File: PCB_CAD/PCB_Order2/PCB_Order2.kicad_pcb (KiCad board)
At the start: 4 copper layers, 48 parts, among them U1 SN74AXCH1T45DCKR, U2 SN74AXCH1T45DCKR

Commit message: moved some stuff on pcb
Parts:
- moved DigitalIn1 99.0 mm to (70.5, 81.7), turned to -90 degrees
- moved C1 90.2 mm to (98.1, 104.6)
- moved C2 90.2 mm to (98.1, 107.6)
- moved C3 90.2 mm to (98.1, 110.6)
- moved C4 90.2 mm to (98.1, 113.6)
- moved C5 90.2 mm to (98.1, 116.6)
- moved C6 90.2 mm to (98.1, 119.6)
- moved C7 90.2 mm to (98.1, 122.6)
- moved C8 90.2 mm to (103.0, 104.6)
- moved DacAnalogSupply_bulk1 90.2 mm to (103.0, 107.6)
- moved DacAnalogSupply_noise1 90.2 mm to (103.0, 110.6)
- moved DacMute_CurrentLimit1 90.2 mm to (102.7, 125.4)
- moved DacOut_L_decouple1 90.2 mm to (103.0, 113.6)
- moved DacOut_L_res1 90.2 mm to (102.7, 127.9)
- moved DacOut_R_decouple1 90.2 mm to (103.0, 116.6)
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
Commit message: continued progress on pcb design
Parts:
- FLASH1, LLSin_ACcouple1, RAM1, SPDIFTX1, SpdifOut_AcCoupling1, SpdifOut_ImpedanceMatch1, llsOut_refHi_noise2, llsOut_refLo_noise1, llsOut_refLo_noise2, uController1: moved to B.Cu
- LLS In1: renamed from U1; moved to B.Cu
- LLS Out1: renamed from U2; moved to B.Cu
- moved AnalogOut1 110.7 mm to (60.5, 131.2), turned to 180 degrees
- moved RAM1 95.3 mm to (141.5, 129.0), turned to 180 degrees
- moved SPDIFTX1 81.1 mm to (140.5, 146.8), turned to 180 degrees
- moved DigitalIn1 80.2 mm to (110.0, 151.5), turned to 180 degrees
- moved AnalogIn1 77.9 mm to (71.5, 146.8), turned to -90 degrees
- moved DigitalOut1 77.3 mm to (125.0, 151.5), turned to 180 degrees
- moved uController1 69.3 mm to (118.5, 129.0), turned to 180 degrees
- moved ADC1 66.9 mm to (100.0, 120.5)
- moved DAC1 64.8 mm to (100.5, 110.0)
- moved SpdifOut_ImpedanceMatch1 54.7 mm to (125.0, 149.5), turned to -90 degrees
- moved Dac_DigitalSup_bulk1 43.5 mm to (86.8, 66.5)
- moved Dac_DigitalSup_noise2 43.5 mm to (86.8, 75.5)
- moved dixSupply_bulk1 43.5 mm to (91.6, 66.5)
- moved C4 43.5 mm to (77.2, 75.5)
- moved C8 43.5 mm to (82.0, 66.5)
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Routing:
- net Net-(DAC1-VREF): track 0.00 -> 9.76 mm
- net Net-(ADC1-VCOM): track 0.00 -> 6.56 mm
- net VDD: track 0.00 -> 4.67 mm, vias 0 -> 1
- net VDD_DIV: track 0.00 -> 4.59 mm
- net GNDD: vias 0 -> 5
- added copper zone on In2.Cu, net (none)
- added copper zone on In2.Cu, net GNDA
- added copper zone on In2.Cu, net GNDD
- added copper zone on In1.Cu, net VDD
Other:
- board outline added: 105.5 x 57 mm
- board text added: "GNDA"
- board text added: "GNDD"

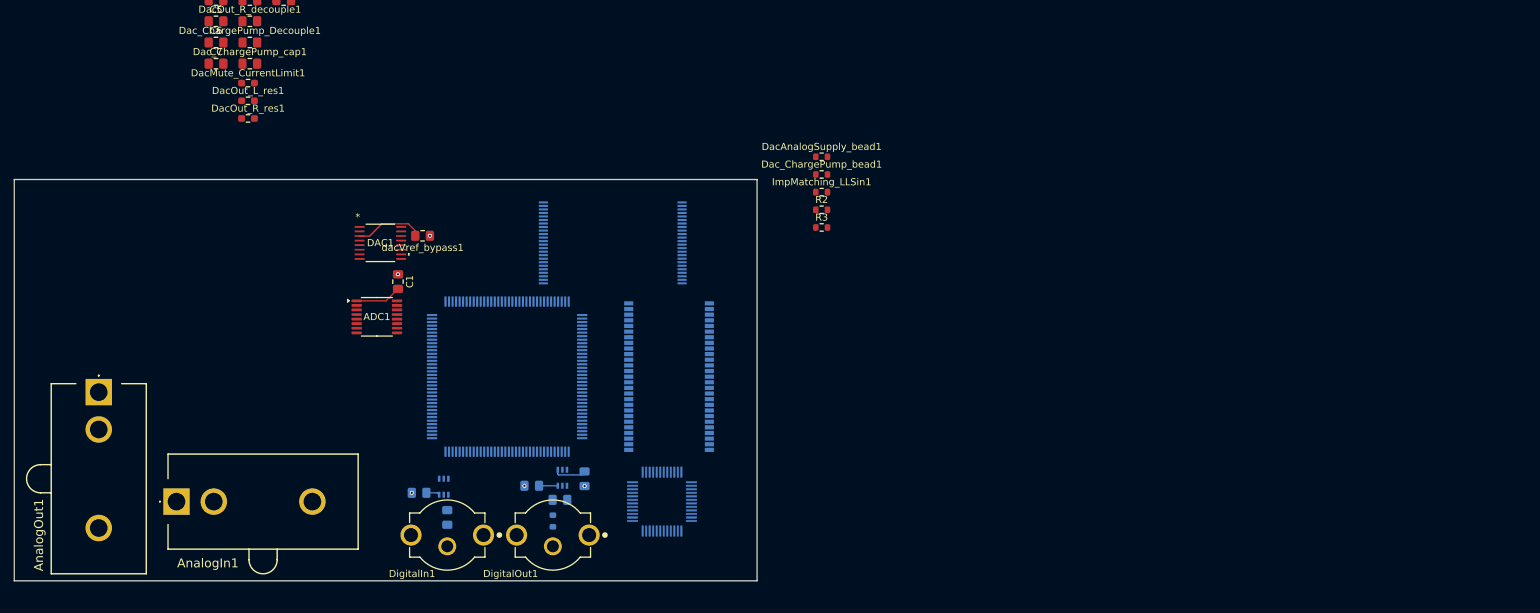
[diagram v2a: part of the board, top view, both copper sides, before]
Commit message: more pcb design things. RAM and Flash wiring
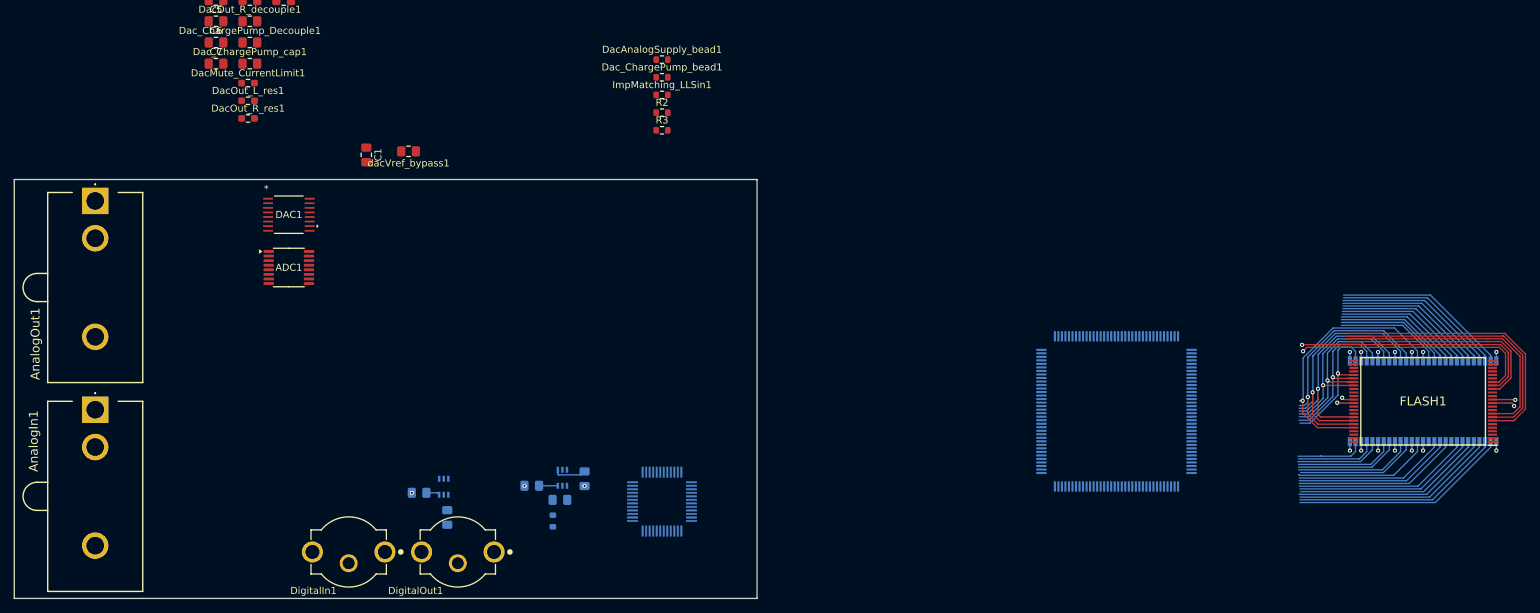
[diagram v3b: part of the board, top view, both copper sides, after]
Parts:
- FLASH1: moved to F.Cu
- moved FLASH1 117.3 mm to (248.6, 132.5), turned to 180 degrees
- moved RAM1 107.2 mm to (248.6, 132.5), turned to -90 degrees
- moved uController1 86.7 mm to (205.1, 133.9), turned to 0 degrees
- moved AnalogOut1 27.2 mm to (60.0, 104.0)
- moved ImpMatching_LLSin1 26.5 mm to (140.5, 89.0)
- moved DacAnalogSupply_bead1 26.5 mm to (140.5, 84.0)
- moved Dac_ChargePump_bead1 26.5 mm to (140.5, 86.5)
- moved R2 26.5 mm to (140.5, 91.5)
- moved R3 26.5 mm to (140.5, 94.0)
- moved C1 18.6 mm to (98.5, 97.5)
- moved AnalogIn1 17.4 mm to (60.0, 133.7), turned to 180 degrees
- moved ADC1 14.3 mm to (87.5, 113.5)
- moved DigitalIn1 14.2 mm to (96.0, 153.9)
- moved DigitalOut1 13.7 mm to (111.5, 153.9)
- moved DAC1 13.6 mm to (87.5, 106.0)
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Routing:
- net /FMC_NWAIT: track 0.00 -> 39.7 mm
- net /FMC_NOE: track 0.00 -> 38.5 mm
- net /FMC_NCE: track 0.00 -> 37.2 mm
- net /FMC_D7: track 0.00 -> 37.1 mm, vias 0 -> 1
- net /FMC_ALE: track 0.00 -> 36.0 mm, vias 0 -> 1
- net /FMC_D6: track 0.00 -> 35.3 mm, vias 0 -> 1
- net /FMC_NWE: track 0.00 -> 34.7 mm, vias 0 -> 1
- net /FMC_D5: track 0.00 -> 34.3 mm, vias 0 -> 1
- net /FMC_D4: track 0.00 -> 31.9 mm, vias 0 -> 1
- net /FMC_A4: track 0.00 -> 31.2 mm
- net /FMC_CLE: track 0.00 -> 31.0 mm
- net /FMC_A5: track 0.00 -> 30.2 mm
- net /FMC_A6: track 0.00 -> 29.2 mm
- net /FMC_A7: track 0.00 -> 28.8 mm
- net /FMC_A8: track 0.00 -> 27.2 mm
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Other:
- board size 105.5 x 57 mm -> 105.5 x 59.5 mm
- board text added: "MUST ADD POWER DECOUPLING TO RAM AND FLASH DO NOT FORGET"

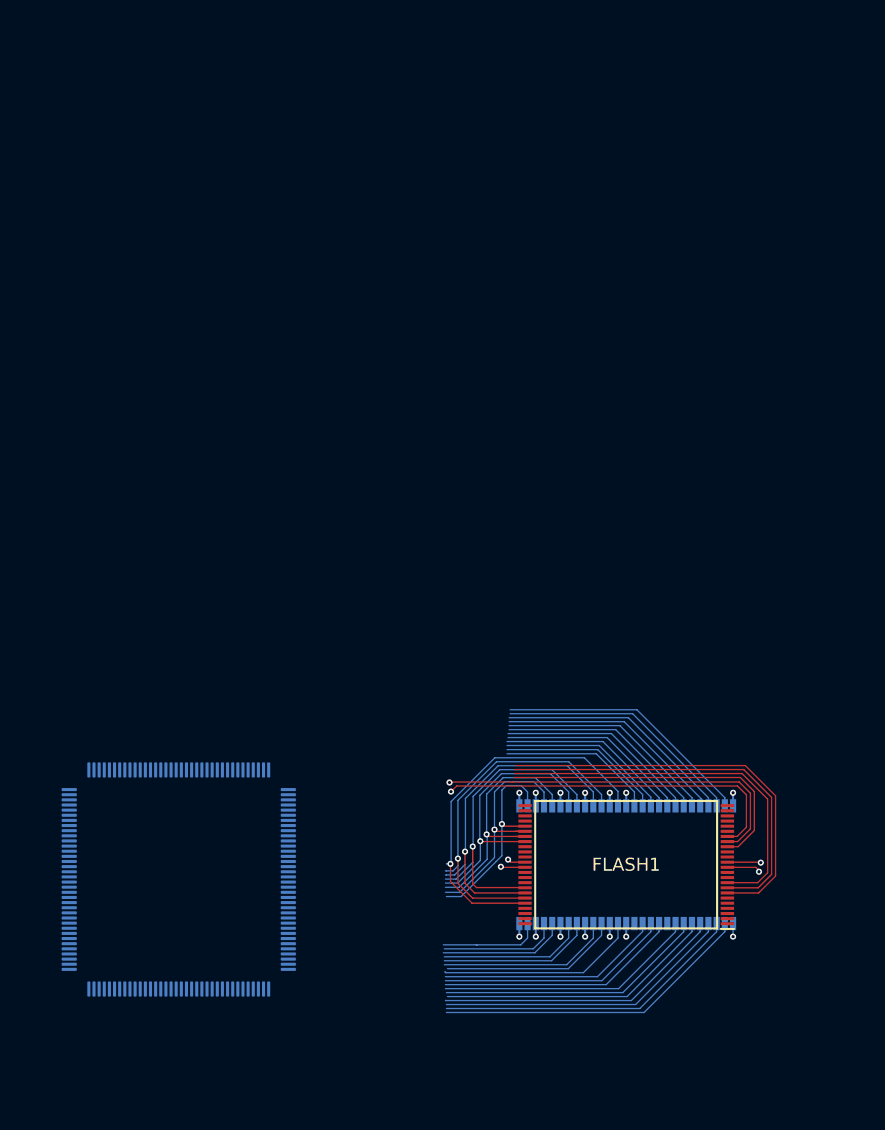
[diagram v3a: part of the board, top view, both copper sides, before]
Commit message: finally found out about manhattan routing. Significant progress made
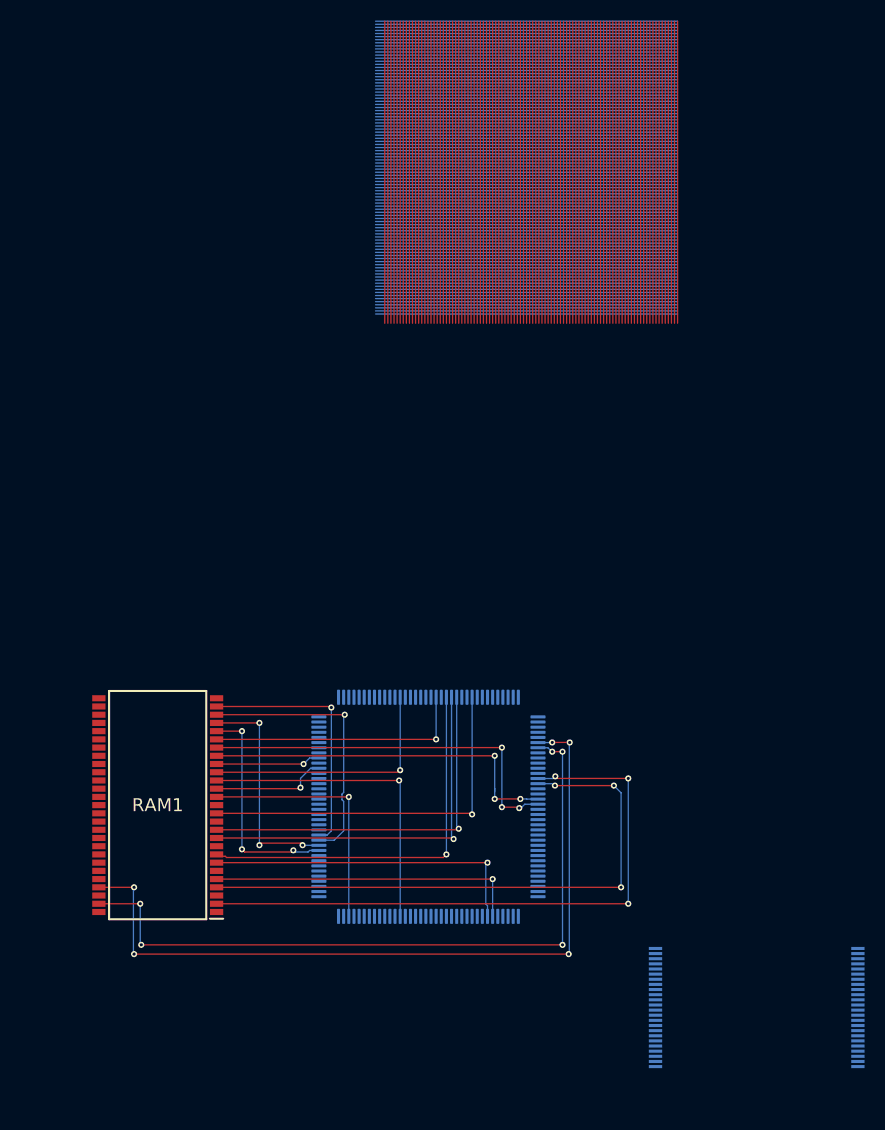
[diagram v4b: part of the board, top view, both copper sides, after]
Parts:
- FLASH1: moved to B.Cu
- RAM1: moved to F.Cu
- moved RAM1 46.0 mm to (203.0, 126.7), turned to 180 degrees
- moved uController1 25.3 mm to (229.3, 126.9)
- moved FLASH1 18.8 mm to (261.3, 146.4), turned to 0 degrees
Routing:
- net (no net): track 0.00 -> 5644.8 mm
- net /FMC_D14: track 11.5 -> 76.0 mm, vias 0 -> 5
- net /FMC_D15: track 9.98 -> 70.5 mm, vias 0 -> 5
- net /FMC_D0: track 20.1 -> 61.2 mm, vias 1 -> 3
- net /FMC_NWAIT: track 39.7 -> 0.00 mm
- net /FMC_NOE: track 38.5 -> 0.00 mm
- net /FMC_NCE: track 37.2 -> 0.00 mm
- net /FMC_ALE: track 36.0 -> 0.00 mm, vias 1 -> 0
- net /FMC_NWE: track 34.7 -> 0.00 mm, vias 1 -> 0
- net /FMC_D1: track 23.6 -> 57.0 mm, vias 1 -> 3
- net /FMC_A4: track 31.2 -> 0.00 mm
- net /FMC_CLE: track 31.0 -> 0.00 mm
- net /FMC_A5: track 30.2 -> 0.00 mm
- net /FMC_A6: track 29.2 -> 0.00 mm
- net /FMC_A7: track 28.8 -> 0.00 mm
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
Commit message: pcb layout stuff
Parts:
- FLASH1: moved to F.Cu
- moved FLASH1 19.1 mm to (256.8, 127.8), turned to 180 degrees
- moved DacAnalogSupply_bead1 12.5 mm to (130.3, 76.7)
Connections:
- RAM1 pad 35: /FMC_11 -> /FMC_A11
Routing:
- net /FMC_D13: track 0.00 -> 79.5 mm, vias 0 -> 3
- net /FMC_SDCLK: track 0.00 -> 78.8 mm, vias 0 -> 3
- net /FMC_D12: track 0.00 -> 75.5 mm, vias 0 -> 3
- net /FMC_D11: track 0.00 -> 72.7 mm, vias 0 -> 3
- net /FMC_D10: track 0.00 -> 69.2 mm, vias 0 -> 3
- net /FMC_D9: track 0.00 -> 66.3 mm, vias 0 -> 3
- net /FMC_D8: track 0.00 -> 62.7 mm, vias 0 -> 3
- net /FMC_NWE: track 0.00 -> 62.3 mm, vias 0 -> 3
- net /FMC_NCE: track 0.00 -> 58.8 mm, vias 0 -> 3
- net /FMC_A4: track 0.00 -> 55.0 mm, vias 0 -> 3
- net /FMC_NOE: track 0.00 -> 53.9 mm, vias 0 -> 3
- net /FMC_NWAIT: track 0.00 -> 53.8 mm, vias 0 -> 3
- net /FMC_A11: track 0.00 -> 50.9 mm, vias 0 -> 3
- net /FMC_A9: track 0.00 -> 47.8 mm, vias 0 -> 3
- net /FMC_SDCKE0: track 0.00 -> 47.0 mm, vias 0 -> 3
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
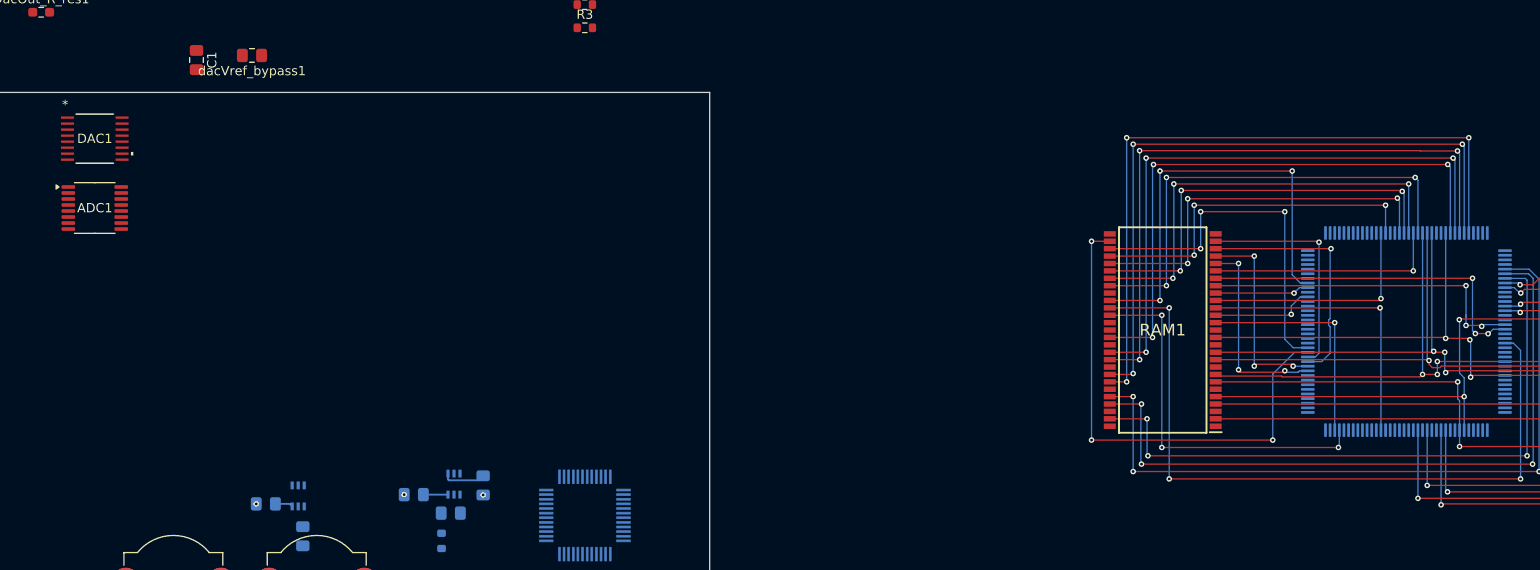
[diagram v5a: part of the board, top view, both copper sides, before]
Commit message: added i2s2 pins on kicad schematic
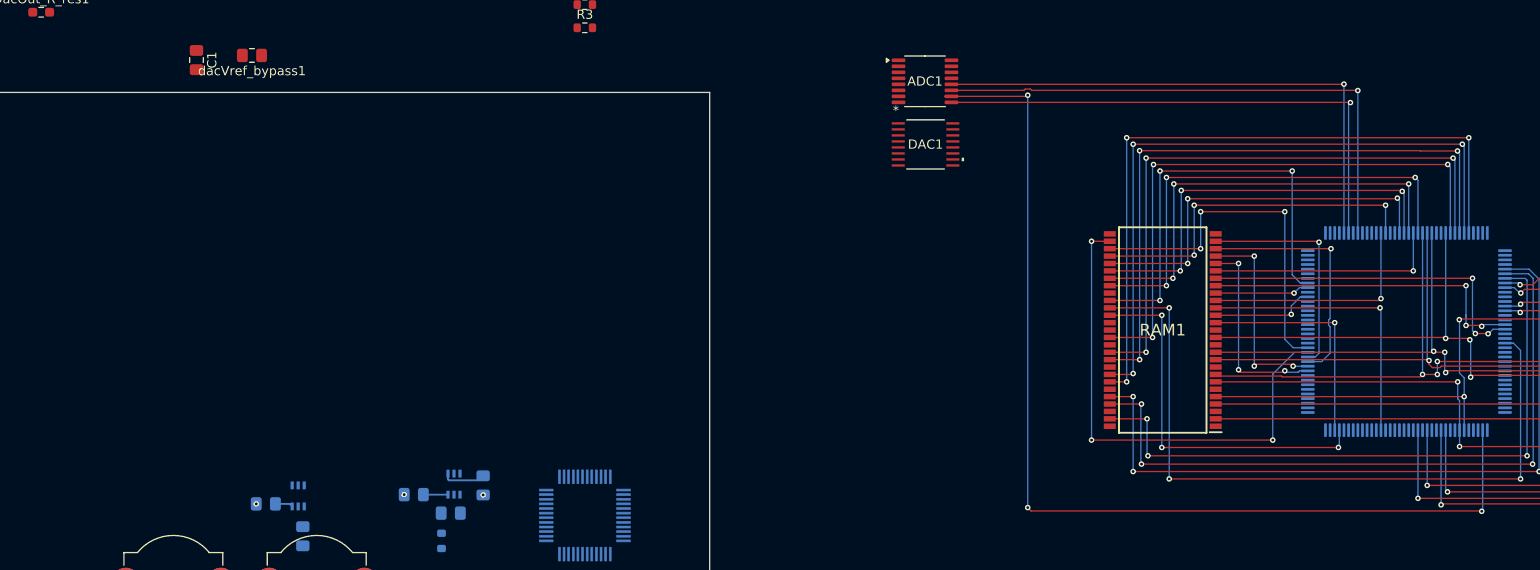
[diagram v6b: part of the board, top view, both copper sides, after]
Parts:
- moved ADC1 90.8 mm to (177.3, 99.8)
- moved DAC1 89.8 mm to (177.3, 106.6)
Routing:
- net /I2S1_WS: track 0.00 -> 112.5 mm, vias 0 -> 3
- net /I2S1_MCK: track 0.00 -> 59.5 mm, vias 0 -> 1
- net /I2S1_CK: track 0.00 -> 58.6 mm, vias 0 -> 1
- net /I2S1_SDI: track 0.00 -> 57.3 mm, vias 0 -> 1
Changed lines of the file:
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@@
 	(footprint "CustomModels:TSSOP16_NAU8402_NUV"
 		(layer "F.Cu")
-		(at 87.5 106)
+		(at 177.34725 106.624993)
 		(tags "NAU8402WG ")
 		(property "Reference" "DAC1"
@@
 	(footprint "Package_SO:TSSOP-16_4.4x5mm_P0.65mm"
 		(layer "F.Cu")
-		(at 87.5 113.5)
+		(at 177.2875 99.8)
 		(descr "TSSOP, 16 Pin (JEDEC MO-153 Var AB https://www.jedec.org/document_search?search_api_views_fulltext=MO-153), generated with kicad-footprint-generator ipc_gullwing_generator.py")
 		(tags "TSSOP SO")
@@
 		(net 0)
 	)
+	(segment
+		(start 188.4 145.9)
+		(end 188.7635 146.2635)
+		(width 0.127)
+		(layer "F.Cu")
+		(net 2)
+	)
+	(segment
+		(start 188.7635 146.2635)
+		(end 237.4635 146.2635)
+		(width 0.127)
+		(layer "F.Cu")
+		(net 2)
+	)
+	(segment
+		(start 180.15 101.425)
+		(end 179.412501 101.425)
+		(width 0.127)
+		(layer "F.Cu")
+		(net 2)
+	)
+	(segment
+		(start 188.275 101.425)
+		(end 188.4 101.3)
+		(width 0.127)
+		(layer "F.Cu")
+		(net 2)
+	)
+	(segment
+		(start 179.412501 101.425)
+		(end 188.275 101.425)
+		(width 0.127)
+		(layer "F.Cu")
+		(net 2)
+	)
+	(segment
+		(start 237.4635 146.2635)
+		(end 237.5 146.3)
+		(width 0.127)
+		(layer "F.Cu")
+		(net 2)
+	)
+	(via
+		(at 188.4 145.9)
+		(size 0.6)
+		(drill 0.3)
+		(layers "F.Cu" "B.Cu")
+		(net 2)
+	)
+	(via
+		(at 188.4 101.3)
+		(size 0.6)
+		(drill 0.3)
+		(layers "F.Cu" "B.Cu")
+		(net 2)
+	)
+	(via
+		(at 237.5 146.3)
+		(size 0.6)
+		(drill 0.3)
+		(layers "F.Cu" "B.Cu")
+		(net 2)
+	)
+	(segment
+		(start 188.4 101.3)
+		(end 188.4 145.9)
+		(width 0.127)
+		(layer "B.Cu")
+		(net 2)
+	)
+	(segment
+		(start 237.5 146.3)
+		(end 237.6 146.2)
+		(width 0.127)
+		(layer "B.Cu")
+		(net 2)
+	)
+	(segment
+		(start 237.6 146.2)
+		(end 237.6 137.525)
+		(width 0.127)
+		(layer "B.Cu")
+		(net 2)
+	)
 	(via blind
 		(at 129.48125 142.48125)
@@
 		(net 4)
 	)
+	(segment
+		(start 223.3 102.1)
+		(end 223.275 102.075)
+		(width 0.127)
+		(layer "F.Cu")
+		(net 5)
+	)
+	(segment
+		(start 223.275 102.075)
+		(end 180.15 102.075)
+		(width 0.127)
+		(layer "F.Cu")
+		(net 5)
+	)
+	(via
+		(at 223.3 102.1)
+		(size 0.6)
+		(drill 0.3)
+		(layers "F.Cu" "B.Cu")
+		(net 5)
+	)
+	(segment
+		(start 223.1 102.3)
+		(end 223.1 116.2)
+		(width 0.127)
+		(layer "B.Cu")
+		(net 5)
+	)
+	(segment
+		(start 223.3 102.1)
+		(end 223.1 102.3)
+		(width 0.127)
+		(layer "B.Cu")
+		(net 5)
+	)
+	(segment
+		(start 222.6 100.1)
+		(end 222.575 100.125)
+		(width 0.127)
+		(layer "F.Cu")
+		(net 9)
+	)
+	(segment
+		(start 222.575 100.125)
+		(end 180.15 100.125)
+		(width 0.127)
+		(layer "F.Cu")
+		(net 9)
+	)
+	(via
+		(at 222.6 100.1)
+		(size 0.6)
+		(drill 0.3)
+		(layers "F.Cu" "B.Cu")
+		(net 9)
+	)
+	(segment
+		(start 222.6 100.1)
+		(end 222.6 116.2)
+		(width 0.127)
+		(layer "B.Cu")
+		(net 9)
+	)
+	(segment
+		(start 188.125169 100.6365)
+		(end 187.986669 100.775)
+		(width 0.127)
+		(layer "F.Cu")
+		(net 10)
+	)
+	(segment
+		(start 188.813331 100.775)
+		(end 188.674831 100.6365)
+		(width 0.127)
+		(layer "F.Cu")
+		(net 10)
+	)
+	(segment
+		(start 188.674831 100.6365)
+		(end 188.125169 100.6365)
+		(width 0.127)
+		(layer "F.Cu")
+		(net 10)
+	)
+	(segment
+		(start 224.1 100.8)
+		(end 224.075 100.775)
+		(width 0.127)
+		(layer "F.Cu")
+		(net 10)
+	)
+	(segment
+		(start 187.986669 100.775)
+		(end 180.15 100.775)
+		(width 0.127)
+		(layer "F.Cu")
+		(net 10)
+	)
+	(segment
+		(start 224.075 100.775)
+		(end 188.813331 100.775)
+		(width 0.127)
+		(layer "F.Cu")
+		(net 10)
+	)
+	(via
+		(at 224.1 100.8)
+		(size 0.6)
+		(drill 0.3)
+		(layers "F.Cu" "B.Cu")
+		(net 10)
+	)
+	(segment
+		(start 224.1 100.8)
+		(end 224.1 116.2)
+		(width 0.127)
+		(layer "B.Cu")
+		(net 10)
+	)
 	(via blind
